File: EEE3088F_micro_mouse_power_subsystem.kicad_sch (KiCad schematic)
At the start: 46 parts, among them J1 Conn_02x16_Odd_Even, J2 Conn_01x02, J3 USB_C_Receptacle_USB2.0_14P, Q1 PMOS, SW1 SW_Omron_B3FS, SW2 HX SS12D10G6, U1 INA219AIDCNR, U2 DRV8833PWPR, U3 DRV8833PWPR, U5 CH224K, U6 TPS82130, U7 TP4056-42-ESOP8, U8 TPTLV70033DDCR, U9 MT3608L

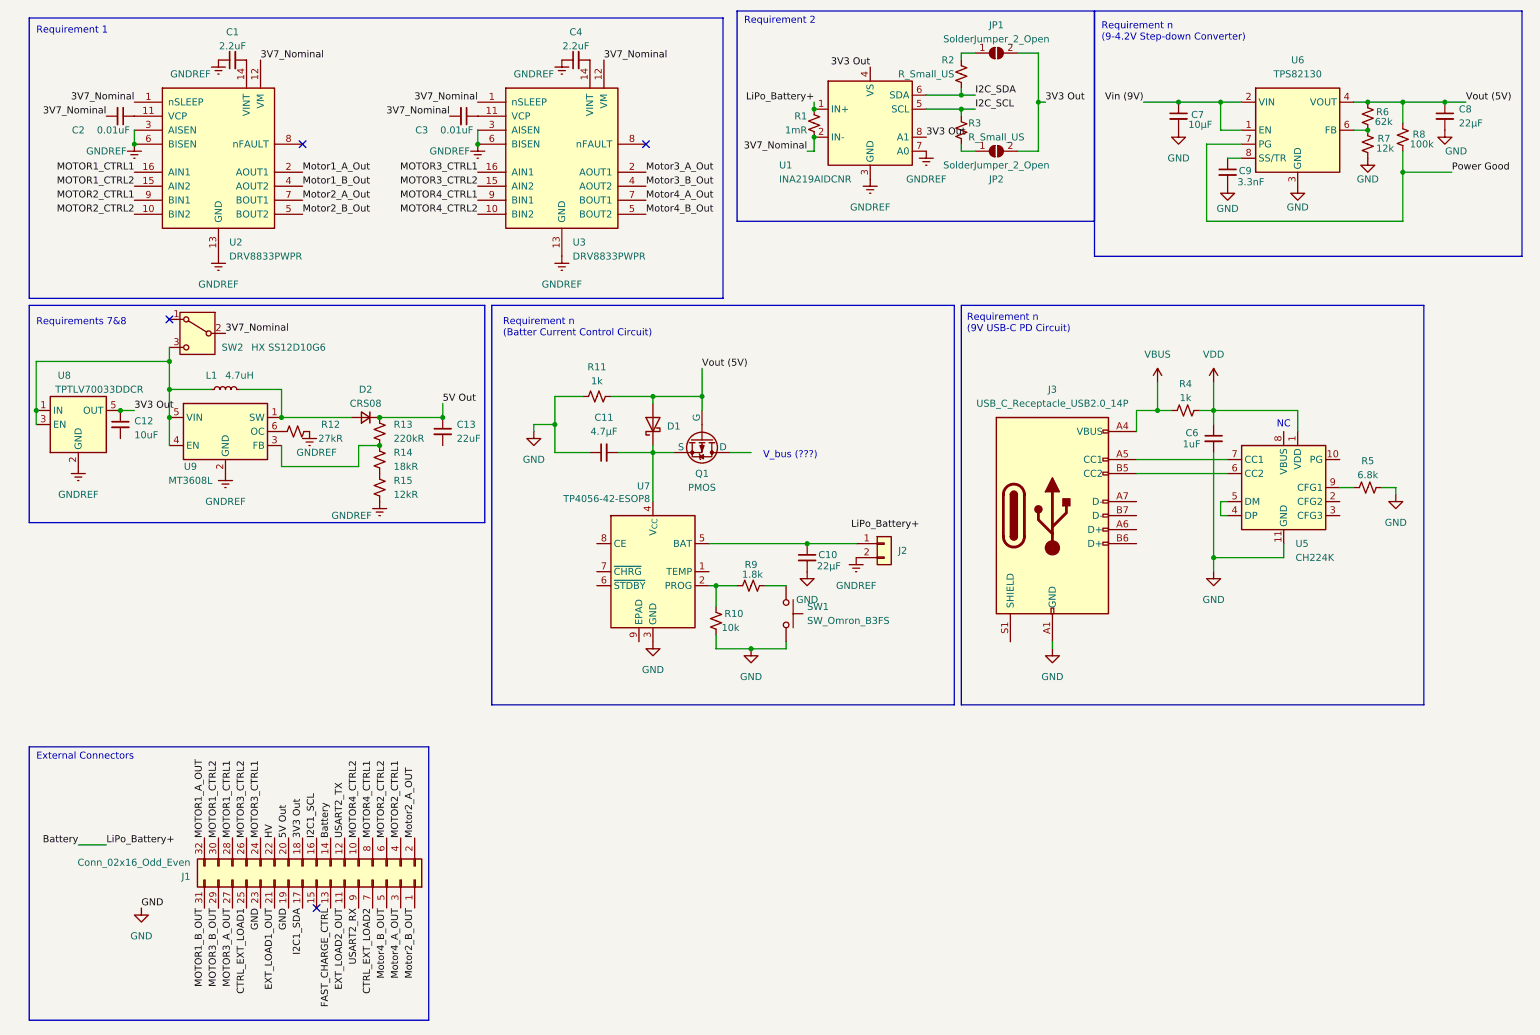
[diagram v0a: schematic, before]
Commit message: Added footprints for half of the components
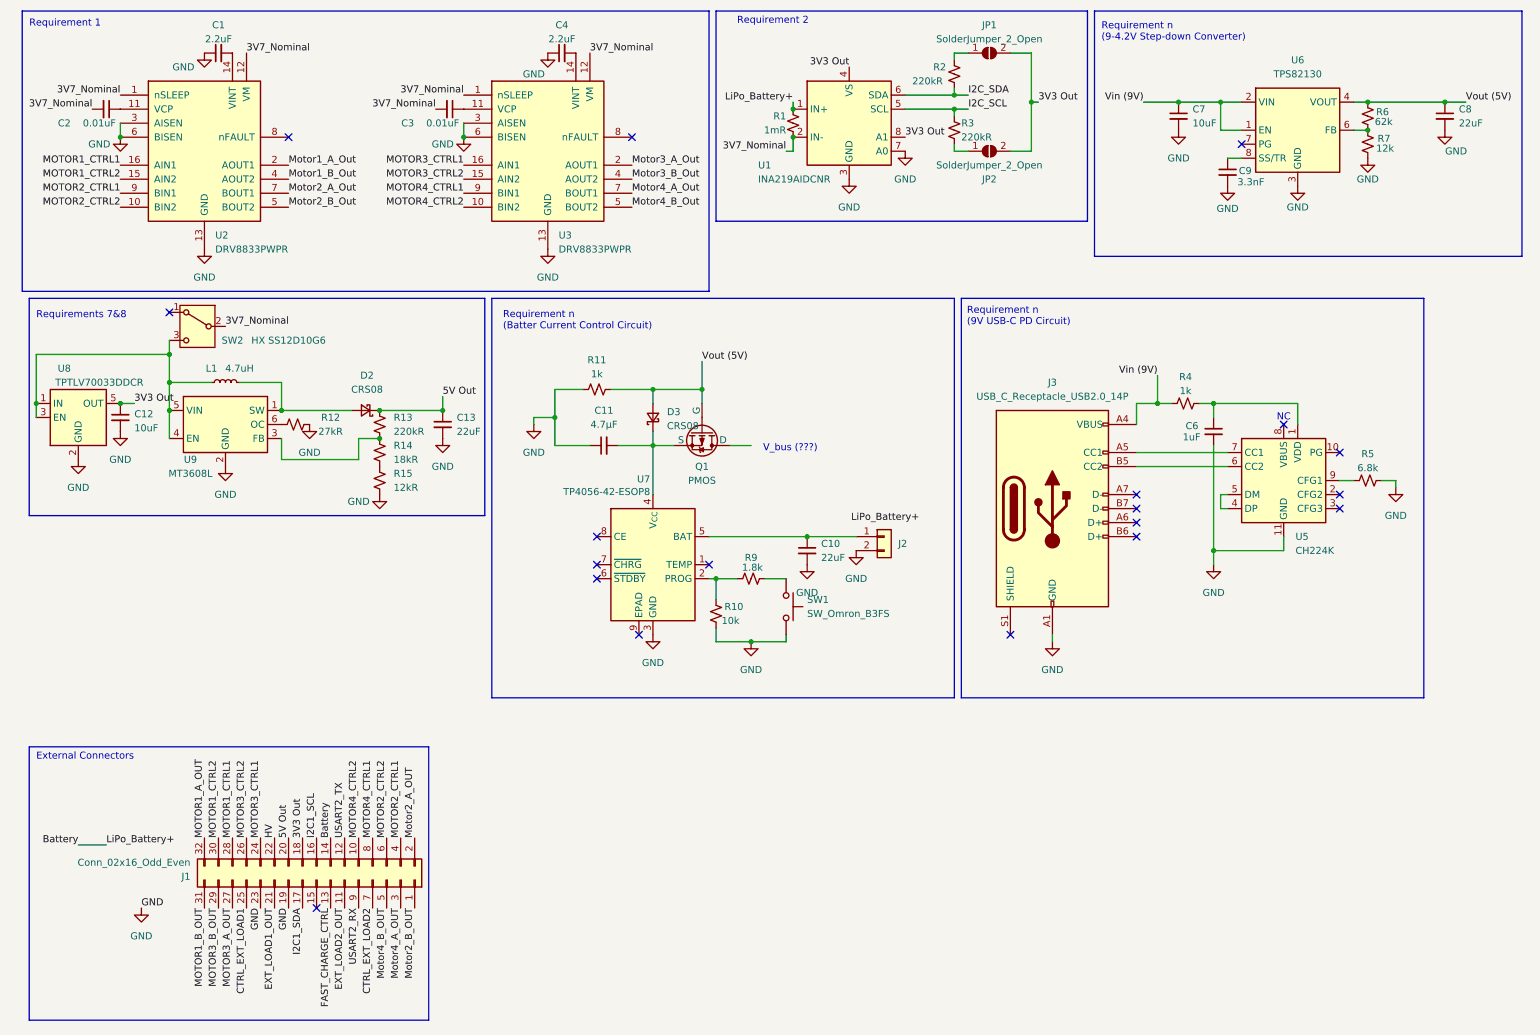
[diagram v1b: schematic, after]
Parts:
- removed D1: D_Schottky, symbol Device:D_Schottky
- removed D2: CRS08, symbol Device:D_Small
- removed R8: 100k, symbol Device:R_Small_US
- added D2, D3: CRS08, Diode_SMD:D_1206_3216Metric, symbol Device:D_Schottky_Small
- C1, C4: footprint (none) -> Capacitor_SMD:C_0402_1005Metric; LCSC (none) -> C12530
- C10, C8: value 22µF -> 22uF; footprint (none) -> Capacitor_SMD:C_0603_1608Metric; LCSC (none) -> C59461
- C12: footprint (none) -> Capacitor_SMD:C_0402_1005Metric
- C13: footprint (none) -> Capacitor_SMD:C_0603_1608Metric
- C2, C3: footprint (none) -> Capacitor_SMD:C_0402_1005Metric; LCSC (none) -> C15195
- C7: value 10µF -> 10uF; footprint (none) -> Capacitor_SMD:C_0402_1005Metric; LCSC (none) -> C15525
- J1: footprint (none) -> Connector_PinSocket_2.54mm:PinSocket_2x16_P2.54mm_Vertical
- J2: footprint (none) -> Connector_JST:JST_PH_S2B-PH-K_1x02_P2.00mm_Horizontal
- JP1, JP2: footprint (none) -> Jumper:SolderJumper-2_P1.3mm_Open_TrianglePad1.0x1.5mm
- L1: footprint (none) -> Inductor_SMD:L_1008_2520Metric
- R1: footprint (none) -> Resistor_SMD:R_1206_3216Metric; LCSC (none) -> C7419993
- R12, R13, R14: footprint (none) -> Resistor_SMD:R_0603_1608Metric
- R15: footprint (none) -> Resistor_SMD:R_0402_1005Metric
- R2, R3: value R_Small_US -> 220kR; footprint (none) -> Resistor_SMD:R_0603_1608Metric; LCSC (none) -> C22961
- R7: footprint (none) -> Resistor_SMD:R_0402_1005Metric; LCSC (none) -> C25752
- SW2: footprint (none) -> Connector_Wire:SolderWire-0.75sqmm_1x03_P4.8mm_D1.25mm_OD2.3mm
- U1: LCSC (none) -> C87469
- U2, U3: LCSC (none) -> C50506
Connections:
- net GNDREF is gone; now on net GND: C1.1, C4.1, J2.2 (Pin_2), R12.2, R15.2, U1.3 (GND), U1.7 (A0), U2.13 (GND), U2.3 (AISEN), U2.6 (BISEN), U3.13 (GND), U3.3 (AISEN), U3.6 (BISEN), U8.2 (GND), U8.4 (GND), U9.2 (GND)
- net VBUS is gone; now on net Vin (9V): J3.A4 (VBUS), J3.A9 (VBUS), J3.B4 (VBUS), J3.B9 (VBUS), R4.2
- net 5V Out: now also D2.1 (K)
- net GND: now also C12.2, C13.2
- net Vout (5V): now also D3.2 (A)
- net at L1.2, U9.1 (SW): now also D2.2 (A)
- net at C11.2, Q1.3 (S), U7.4 (V_{CC}): now also D3.1 (K)
- net Power Good: no longer names the net of U6.7 (PG)
- net VDD: no longer names the net of C6.1, R4.1, U5.1 (VDD)
- no-connect marks 4 -> 19
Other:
- moved on the sheet: C1, C11, C12, C13, C2, C6, J2, J3, JP1, JP2, L1, Q1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

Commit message: Final changes to schematic and footprints
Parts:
- removed SW1: SW_Omron_B3FS, symbol Switch:SW_Omron_B3FS
- added Q2, Q3: PMOS, Package_TO_SOT_SMD:SOT-23, symbol Simulation_SPICE:PMOS
- added Q4: NMOS, Package_TO_SOT_SMD:SOT-23, symbol Simulation_SPICE:NMOS
- added R16, R22, R23: 1k, Resistor_SMD:R_1206_3216Metric, symbol Device:R_Small_US
- added R17, R21: 100R, Resistor_SMD:R_0805_2012Metric, symbol Device:R_Small_US
- added R18, R8: 10k, Resistor_SMD:R_0603_1608Metric, symbol Device:R_Small_US
- added R19: 20k, Resistor_SMD:R_0603_1608Metric, symbol Device:R_Small_US
- added R20: 22k, Resistor_SMD:R_0603_1608Metric, symbol Device:R_Small_US
- added U4: TC4426xOA, Package_SO:SOIC-8_3.9x4.9mm_P1.27mm, symbol Driver_FET:TC4426xOA
- C11: footprint (none) -> Capacitor_SMD:C_0805_2012Metric; LCSC (none) -> C1779
- C6: footprint (none) -> Capacitor_SMD:C_0402_1005Metric; LCSC (none) -> C1848
- C9: footprint (none) -> Capacitor_SMD:C_0603_1608Metric; LCSC (none) -> C1613
- J3: footprint (none) -> Connector_USB:USB_C_Receptacle_Amphenol_12401948E412A; LCSC (none) -> C3151746
- Q1: footprint (none) -> Package_TO_SOT_SMD:SOT-23; LCSC (none) -> C5224173
- R10: footprint (none) -> Resistor_SMD:R_0603_1608Metric; Field5 (none) -> C25804
- R11: value 1k -> 10k; footprint (none) -> Resistor_SMD:R_0603_1608Metric; Field5 (none) -> C25804
- R4: footprint (none) -> Resistor_SMD:R_1206_3216Metric; LCSC (none) -> C4410
- R5: footprint (none) -> Resistor_SMD:R_0805_2012Metric; LCSC (none) -> C17772
- R6: value 62k -> 20k; footprint (none) -> Resistor_SMD:R_0603_1608Metric; LCSC (none) -> C4184
- R9: value 1.8k -> 3.3k; footprint (none) -> Resistor_SMD:R_0603_1608Metric; LCSC (none) -> C22978
- U5: LCSC (none) -> C970725
- U6: LCSC (none) -> C473914
- U7: LCSC (none) -> C21417
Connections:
- net CTRL_EXT_LOAD1: now also U4.2 (IN_A)
- net CTRL_EXT_LOAD2: now also U4.4 (IN_B)
- net EXT_LOAD1_OUT: now also Q2.1 (D)
- net EXT_LOAD2_OUT: now also Q3.1 (D)
- net FAST_CHARGE_CTRL: now also R23.1
- net GND: now also R10.2, R11.2, U7.1 (TEMP), Q4.3 (S), R16.2, U4.3 (GND); no longer R10.1, R11.1
- net HV: now also J3.A4 (VBUS), J3.A9 (VBUS), J3.B4 (VBUS), J3.B9 (VBUS), R4.2
- net Vin (9V): now also Q1.1 (D); no longer J3.A4 (VBUS), J3.A9 (VBUS), J3.B4 (VBUS), J3.B9 (VBUS), R4.2
- net Vout (5V): now also Q2.3 (S), Q3.3 (S), R16.1, R18.1, R22.2, R8.1, U4.6 (VDD); no longer R11.2
- net at R9.1, U7.2 (PROG): now also R10.1, R11.1; no longer R10.2
- net at R9.2: now also Q4.1 (D)
- net at U7.8 (CE): now also R22.1
- net at R7.1, U6.6 (FB): now also R20.2; no longer R6.2
- new net: R19.1, R6.2
- new net: R19.2, R20.1
- new net: Q4.2 (G), R23.2
- new net: Q3.2 (G), R17.2, R18.2
- new net: Q2.2 (G), R21.2, R8.2
- new net: R21.1, U4.7 (~{OUT_A})
- new net: R17.1, U4.5 (~{OUT_B})
- no-connect marks 19 -> 17
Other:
- note added: "2x High side switch"
- note removed: "V_bus (???)"
- moved on the sheet: R7

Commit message: Created PCB layout and production files
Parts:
- removed D3: CRS08, Diode_SMD:D_1206_3216Metric, symbol Device:D_Schottky_Small
- added D1: 1N4734A-TAP, Diode_THT:D_DO-35_SOD27_P2.54mm_Vertical_AnodeUp, symbol Device:D_Zener_Small
- J1: footprint Connector_PinSocket_2.54mm:PinSocket_2x16_P2.54mm_Vertical -> Connector_PinHeader_2.54mm:PinHeader_2x16_P2.54mm_Vertical
- J3: footprint Connector_USB:USB_C_Receptacle_Amphenol_12401948E412A -> Connector_USB:USB_C_Receptacle_GCT_USB4125-xx-x-0190_6P_TopMnt_Horizontal; LCSC C3151746 -> C168701
- Q3: LCSC (none) -> C5224173
- Q4: LCSC C8545 -> C8545
- R10, R11, R18, R8: Field5 C25804 -> (none); LCSC (none) -> C25804
- U5: LCSC C970725 -> C970725
- U7: LCSC C21417 -> C21417
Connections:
- net I2C_SCL is gone; now on net I2C1_SCL: R3.1, U1.5 (SCL)
- net I2C_SDA is gone; now on net I2C1_SDA: R2.2, U1.6 (SDA)
- net Motor1_A_Out is gone; now on net MOTOR1_A_OUT: U2.2 (AOUT1)
- net Motor1_B_Out is gone; now on net MOTOR1_B_OUT: U2.4 (AOUT2)
- net Motor2_A_Out is gone; now on net MOTOR3_A_OUT: U2.7 (BOUT1)
- net Motor2_B_Out is gone; now on net MOTOR3_B_OUT: U2.5 (BOUT2)
- net Motor3_A_Out is gone; now on net Motor2_A_OUT: U3.2 (AOUT1)
- net Motor3_B_Out is gone; now on net Motor2_B_OUT: U3.4 (AOUT2)
- net Motor4_A_Out is gone; now on net Motor4_A_OUT: U3.7 (BOUT1)
- net Motor4_B_Out is gone; now on net Motor4_B_OUT: U3.5 (BOUT2)
- net Vin (9V) is gone; now on net HV: C7.1, Q1.1 (D), U6.1 (EN), U6.2 (VIN)
- net 5V Out: now also Q2.3 (S), Q3.3 (S), R18.1, R8.1, U4.6 (VDD)
- net Battery: now also C10.1, J2.2 (Pin_1), U7.5 (BAT)
- net FAST_CHARGE_CTRL: now also R23.2; no longer R23.1
- net GND: now also J2.1 (Pin_2), U7.9 (EPAD); no longer J2.2 (Pin_2), J3.A1 (GND)
- net HV: no longer J3.A4 (VBUS)
- net MOTOR2_CTRL1: now also U3.16 (AIN1); no longer U2.9 (BIN1)
- net MOTOR2_CTRL2: now also U3.15 (AIN2); no longer U2.10 (BIN2)
- net MOTOR3_CTRL1: now also U2.9 (BIN1); no longer U3.16 (AIN1)
- net MOTOR3_CTRL2: now also U2.10 (BIN2); no longer U3.15 (AIN2)
- net Vout (5V): now also D1.2 (A); no longer Q2.3 (S), Q3.3 (S), R18.1, R8.1, U4.6 (VDD)
- net at C11.2, Q1.3 (S), U7.4 (V_{CC}): now also D1.1 (K)
- net at Q4.2 (G): now also R23.1; no longer R23.2
- no-connect marks 17 -> 12
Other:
- title: Micro Mouse Power Subsystem -> Micro Mouse Power Subsystem Schematic
- moved on the sheet: R23
